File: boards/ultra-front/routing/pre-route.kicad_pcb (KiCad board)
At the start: 2 copper layers, 110 x 40 mm, 40 parts, among them J1 FPC-05F-20PH20, J2 FPC-05FB-12PH20, Q1 AO3400A, SW1 TS-1187A-B-A-B, SW2 TS-1187A-B-A-B, SW3 TS-1187A-B-A-B, SW4 EC11E1834403, U1 TCA9535PWR, U2 IRM-H638T/TR2

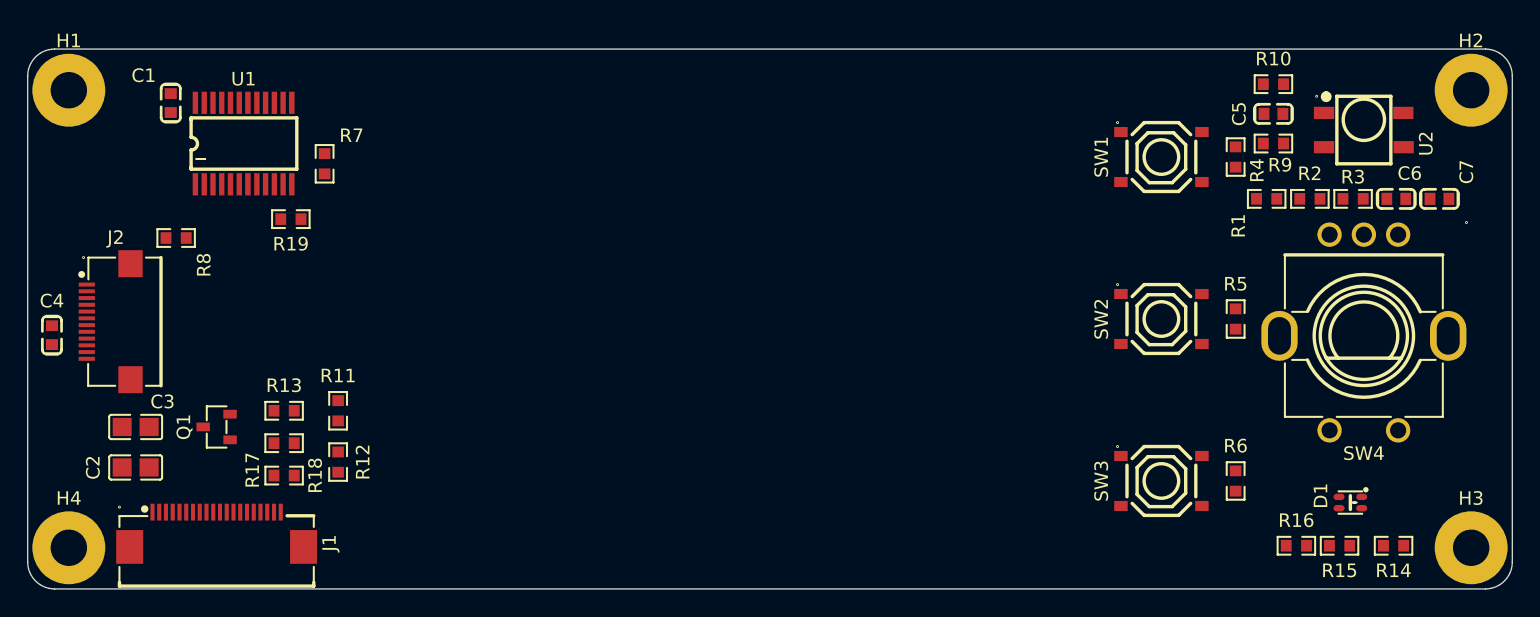
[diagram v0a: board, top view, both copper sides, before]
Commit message: ultra-front: fix LCD tail seating and keepouts from board review, re-route (GND as a net, edge keepout), docs and learnings
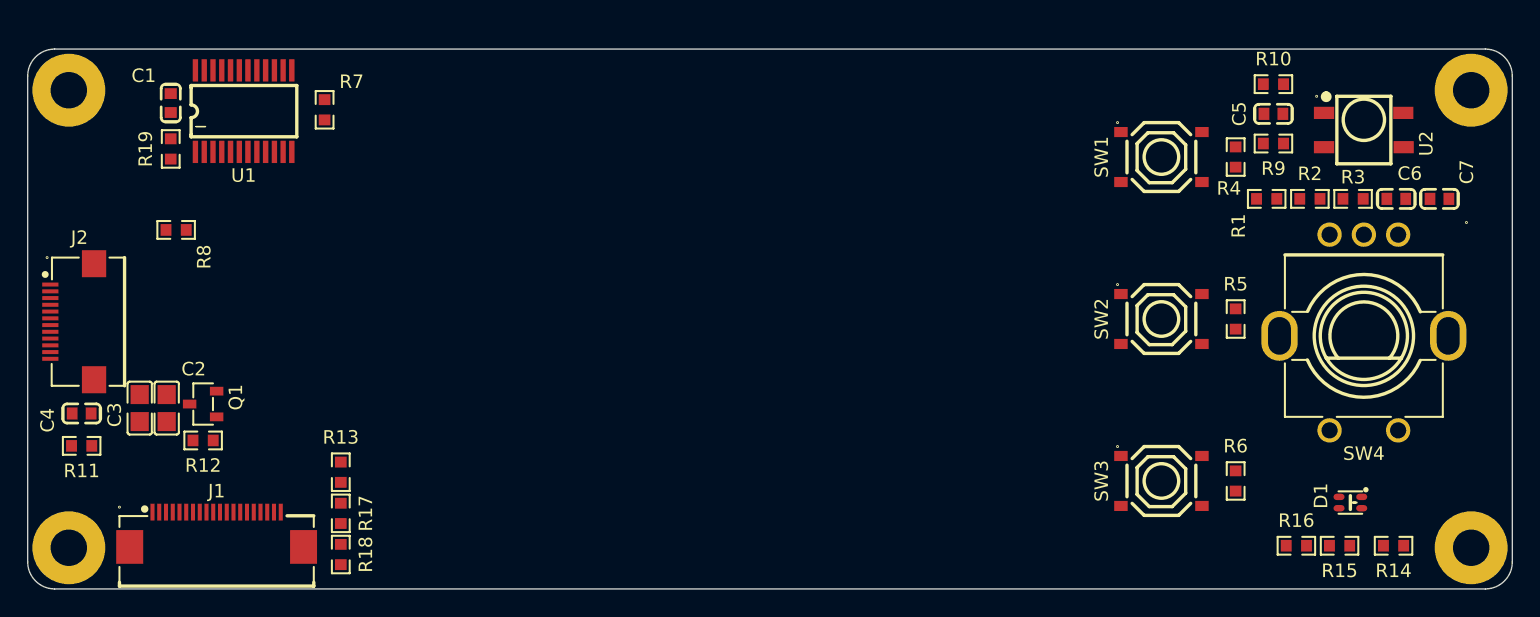
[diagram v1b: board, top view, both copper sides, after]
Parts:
- moved R11 19.2 mm to (-5.95, 56.2), turned to 0 degrees
- moved R19 10.3 mm to (0.66, 34.2), turned to 90 degrees
- moved R12 10.1 mm to (3.06, 55.8), turned to 0 degrees
- moved R18 7.20 mm to (13.3, 64.2), turned to 90 degrees
- moved R17 6.68 mm to (13.3, 61.2), turned to 90 degrees
- moved C4 6.20 mm to (-5.95, 53.8), turned to 0 degrees
- moved R13 6.19 mm to (13.3, 58.1), turned to 90 degrees
- moved C2 4.96 mm to (0.35, 53.4), turned to 90 degrees
- moved R7 4.00 mm to (12.1, 31.3)
- moved J2 2.70 mm to (-6.64, 47.0)
- moved U1 2.40 mm to (6.05, 31.4)
- moved Q1 1.97 mm to (3.06, 53.1)
- moved C3 1.43 mm to (-1.65, 53.4), turned to 90 degrees
- moved R8 0.60 mm to (1.05, 40.2)
